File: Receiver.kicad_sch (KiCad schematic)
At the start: 18 parts, among them J3 ReceiverData, J4 ReceiverRS485, U11 MAX485E, U13 LM7805

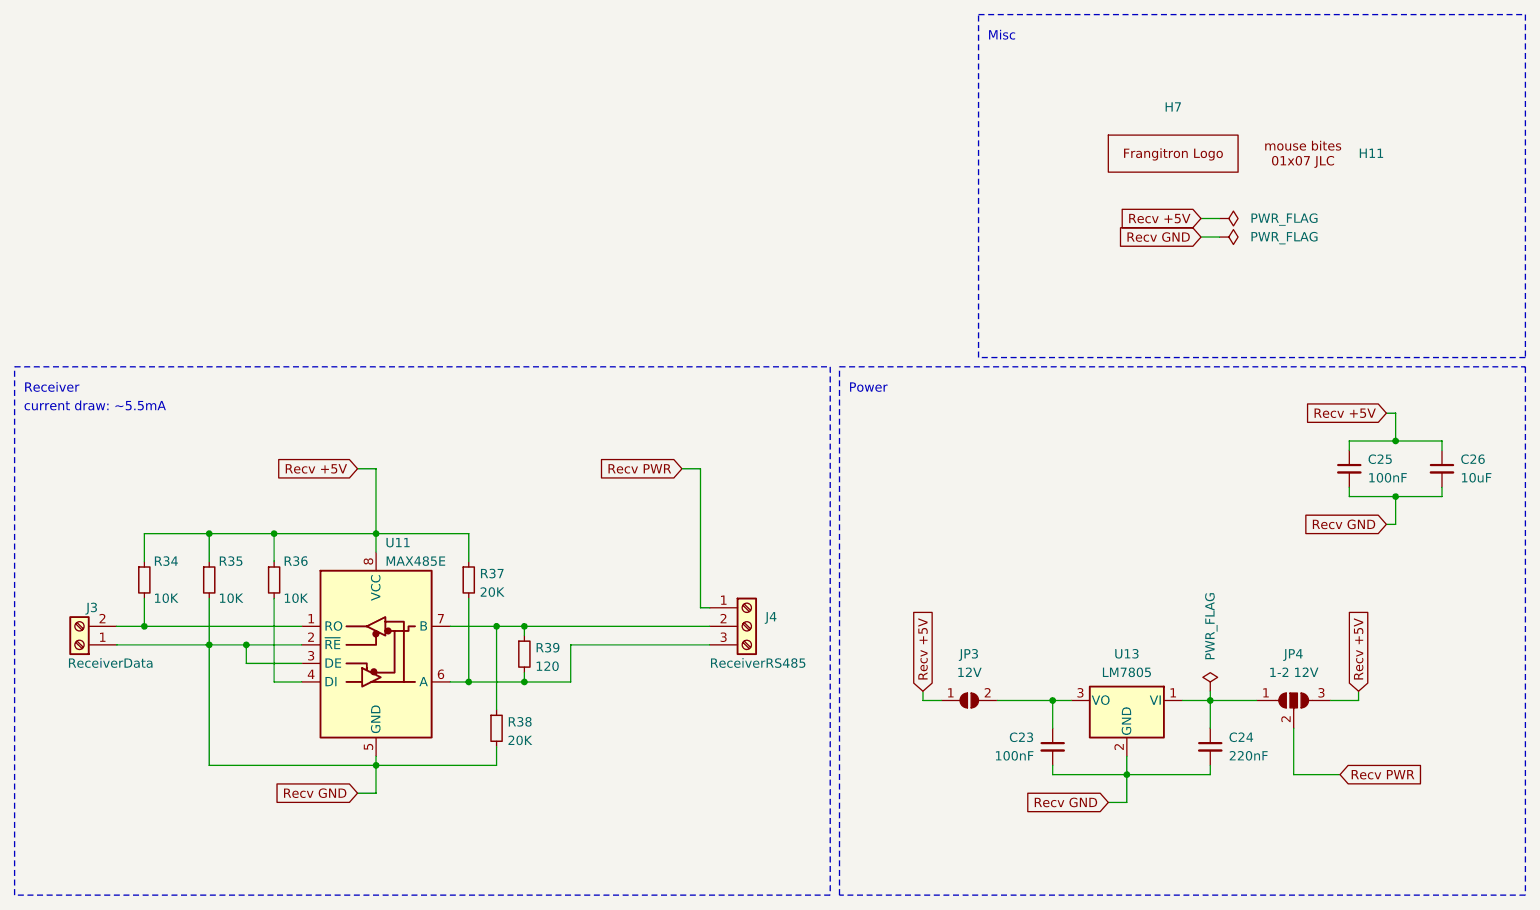
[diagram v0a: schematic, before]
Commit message: receiver layout OK, some references fixed
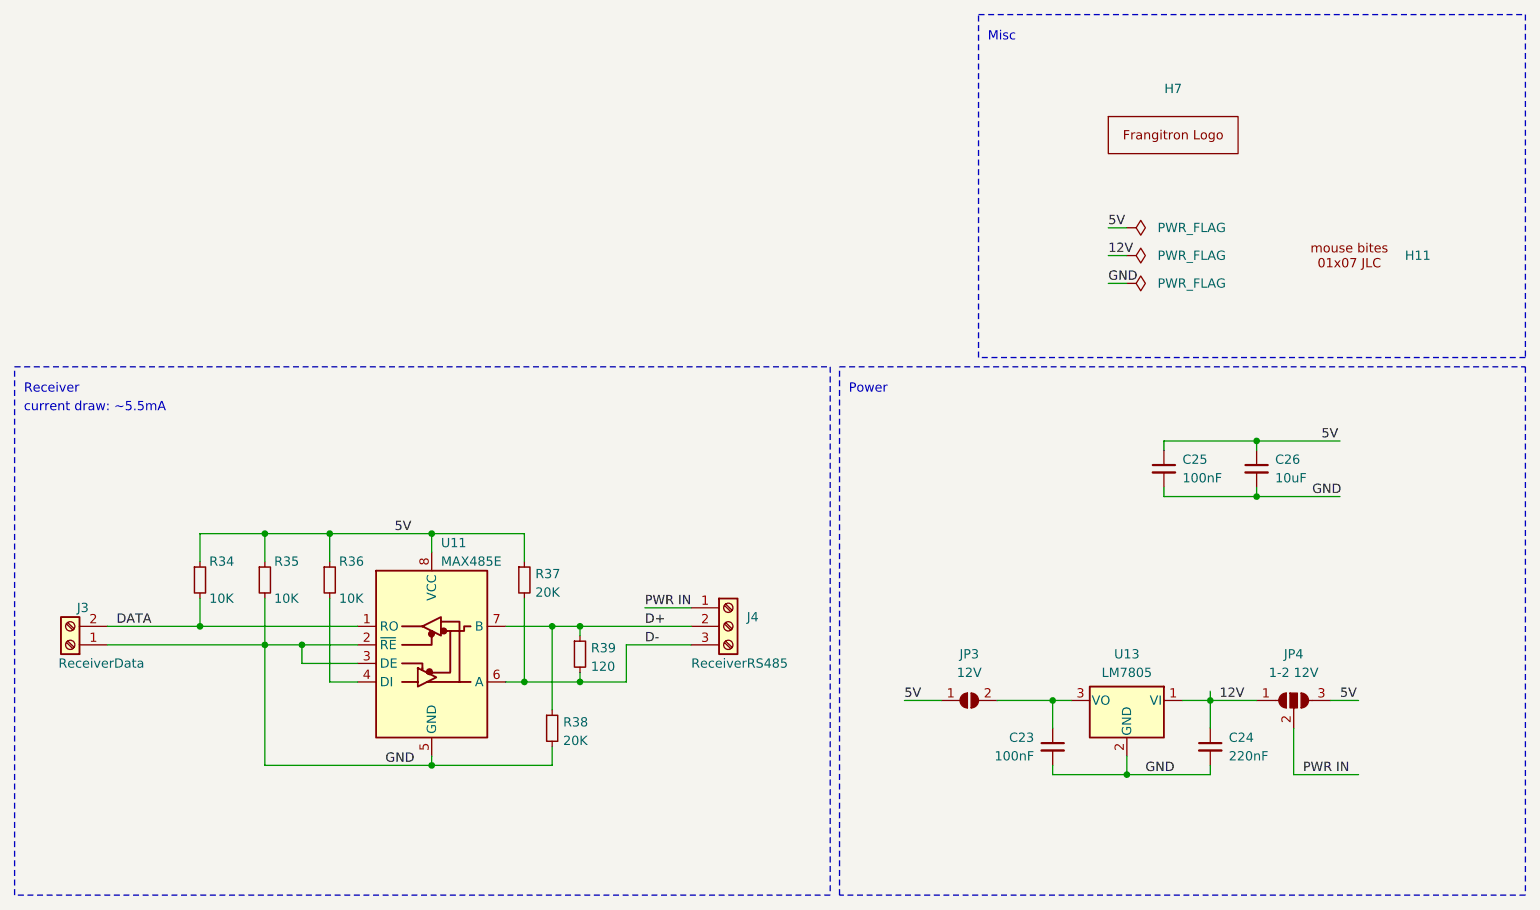
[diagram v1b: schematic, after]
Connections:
- net D+: now reaches J4.2 (Pin_2), R38.1, R39.1, U11.7 (B)
- net D-: now reaches J4.3 (Pin_3), R37.2, R39.2, U11.6 (A)
- net 12V: now reaches C24.1, JP4.1 (A), U13.1 (VI)
- net DATA: now reaches J3.2 (Pin_2), R34.2, U11.1 (RO)
- net Recv +5V renamed 5V
- net Recv GND renamed GND
- net Recv PWR renamed PWR IN
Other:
- moved on the sheet: C25, C26, H11, H7, J3, J4, R34, R35, R36, R37, R38, R39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

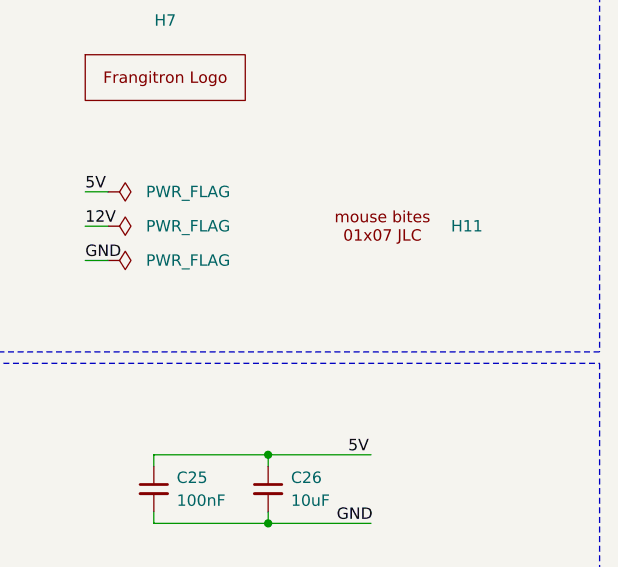
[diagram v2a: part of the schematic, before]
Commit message: panelization with only mouse bites, routing finished
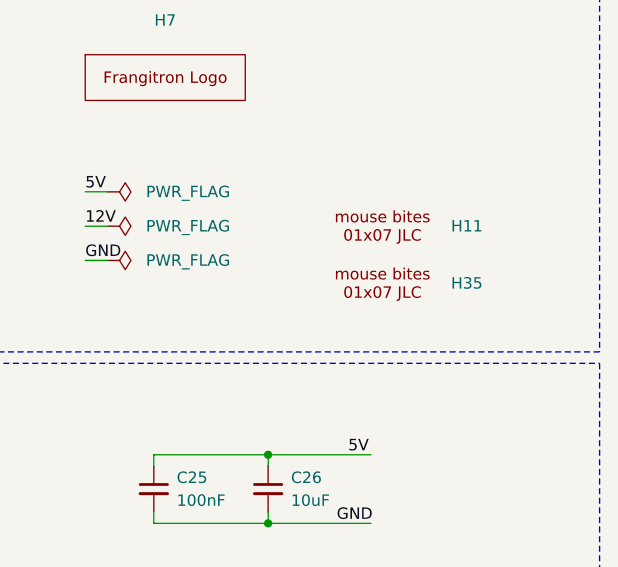
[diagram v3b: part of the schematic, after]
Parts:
- added H35: ~, Library:mouse-bites-1x07-jlc, symbol Library:mouse-bites-1x07-jlc
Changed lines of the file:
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@@
+    )
+  )
+  (symbol (lib_id "Library:mouse-bites-1x07-jlc") (at 224.79 68.58 0) (unit 1)
+    (in_bom yes) (on_board yes) (dnp no) (fields_autoplaced)
+    (property "Reference" "H35" (at 232.41 68.58 0)
+      (effects (font (size 1.27 1.27)) (justify left))
+    )
+    (property "Value" "~" (at 224.79 68.58 0)
+      (effects (font (size 1.27 1.27)))
+    )
+    (property "Footprint" "Library:mouse-bites-1x07-jlc" (at 224.79 68.58 0)
+      (effects (font (size 1.27 1.27)) hide)
+    )
+    (property "Datasheet" "" (at 224.79 68.58 0)
+      (effects (font (size 1.27 1.27)) hide)
+    )
+    (instances
+      (project "rp2040-led-board-schematics-v02"
+        (path "/c1a38541-3f06-4b3b-ba3a-decae3ac3c31/757d6d50-47c9-4cb1-8547-9b2447e826a6"
+          (reference "H35") (unit 1)
+        )
+        (path "/c1a38541-3f06-4b3b-ba3a-decae3ac3c31/c0d607bf-2e76-4853-b2ed-907dd6c894fe"
+          (reference "H36") (unit 1)
+        )
+        (path "/c1a38541-3f06-4b3b-ba3a-decae3ac3c31/45693edd-6dc6-41b8-8b1c-a9a8e5afcadf"
+          (reference "H37") (unit 1)
+        )
+        (path "/c1a38541-3f06-4b3b-ba3a-decae3ac3c31/50d6fe7a-2d25-4b6a-8e40-e76ae84b788d"
+          (reference "H38") (unit 1)
+        )
+        (path "/c1a38541-3f06-4b3b-ba3a-decae3ac3c31/62e0dde2-ad5d-4205-a74c-f24b413f3931"
+          (reference "H39") (unit 1)
+        )
+        (path "/c1a38541-3f06-4b3b-ba3a-decae3ac3c31/25bef58f-ca62-4f18-ad32-cc60a54b91e0"
+          (reference "H40") (unit 1)
+        )
+        (path "/c1a38541-3f06-4b3b-ba3a-decae3ac3c31/507a174b-d652-466e-bcdb-3655449e938c"
+          (reference "H41") (unit 1)
+        )
+        (path "/c1a38541-3f06-4b3b-ba3a-decae3ac3c31/ceb5b469-5e62-41bb-a8f0-8c2a1861cc28"
+          (reference "H42") (unit 1)
+        )
+      )
     )
   )

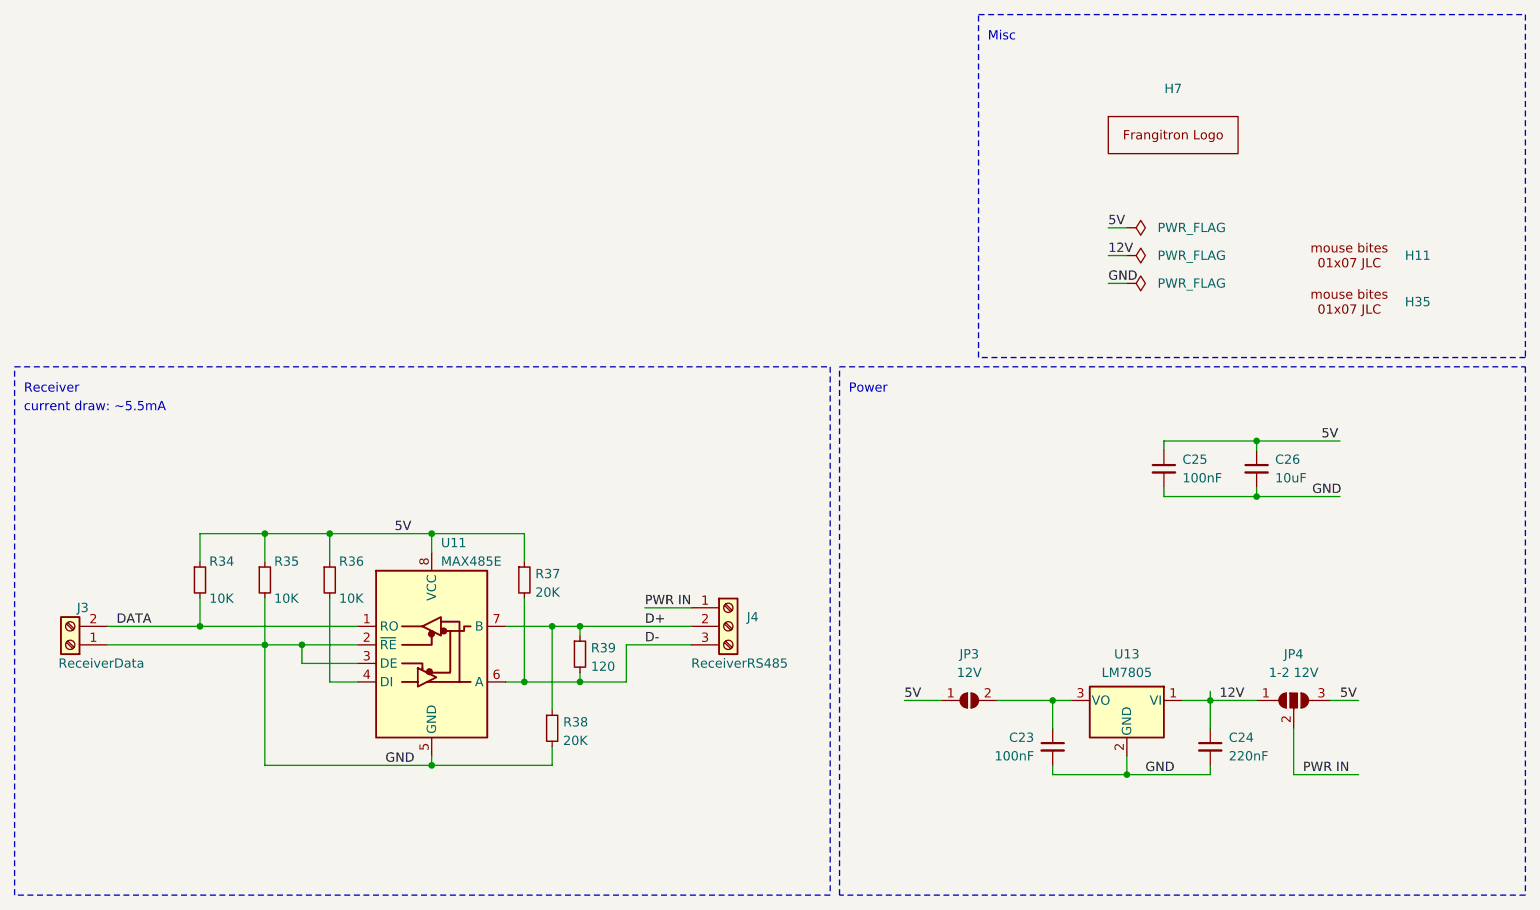
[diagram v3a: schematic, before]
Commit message: Geographically reannotate
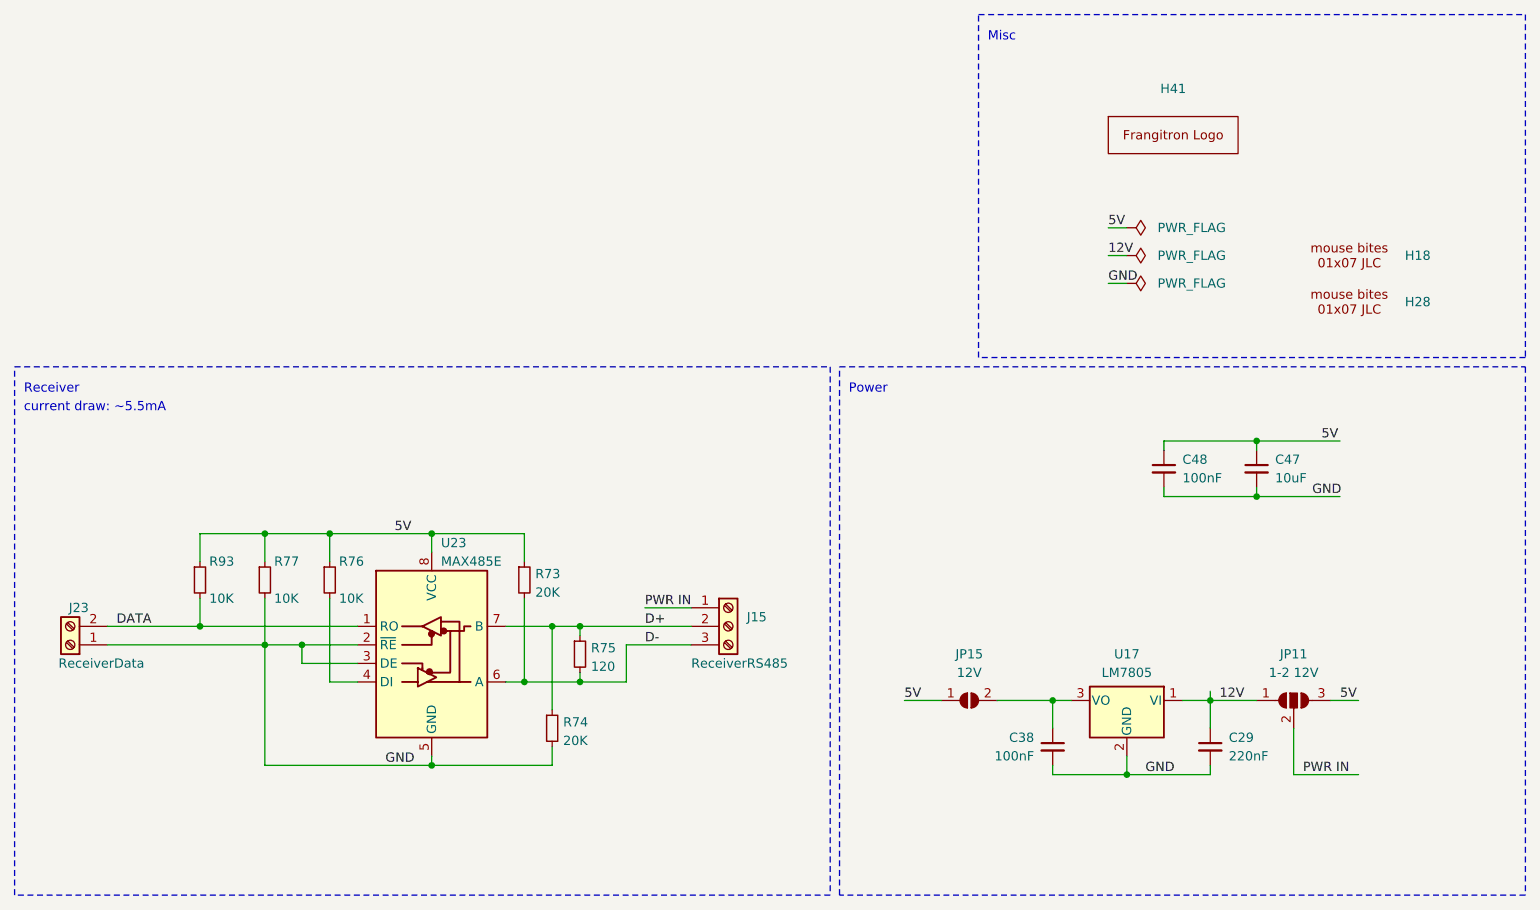
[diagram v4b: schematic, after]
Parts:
- C47: renamed from C26; footprint Capacitor_SMD:C_0402_1005Metric -> Capacitor_SMD:C_0603_1608Metric
- renumbered C24 to C29, C23 to C38, C25 to C48, H11 to H18, H35 to H28, H7 to H41, J4 to J15, J3 to J23, JP4 to JP11, JP3 to JP15, R37 to R73, R38 to R74, R39 to R75, R36 to R76, R35 to R77, R34 to R93, U13 to U17, U11 to U23

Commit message: fix power sources, update reveivers accordingly (main board PCB not updated yet)
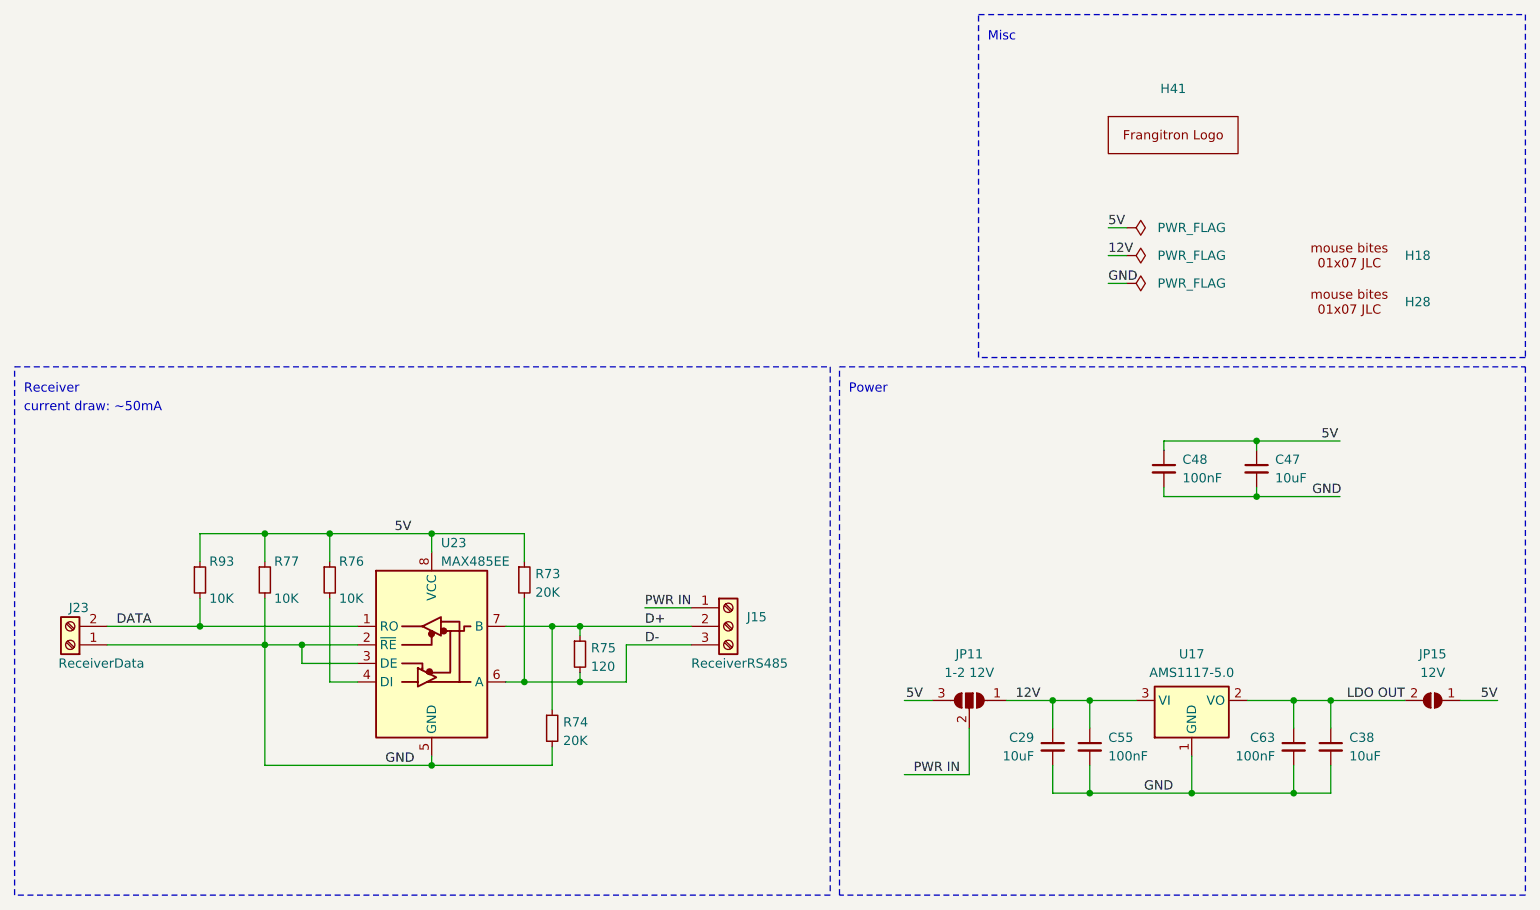
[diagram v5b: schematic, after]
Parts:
- removed U17: LM7805, Package_TO_SOT_SMD:SOT-223, symbol Regulator_Linear:LM7805_TO220
- added C55, C63: 100nF, Capacitor_SMD:C_0603_1608Metric, symbol Device:C_Small
- added U17: AMS1117-5.0, Package_TO_SOT_SMD:SOT-223-3_TabPin2, symbol Regulator_Linear:AMS1117-5.0
- C29: value 220nF -> 10uF; LCSC Part # C1525 -> (none); LCSC Part Number C1525 -> (none)
- C38: value 100nF -> 10uF; LCSC Part # C1525 -> (none); LCSC Part Number C1525 -> (none)
- C47, C48: LCSC Part # C1525 -> (none); LCSC Part Number C1525 -> (none)
- R73, R74, R75: LCSC Part # C4328 -> (none); LCSC Part Number C4328 -> (none)
- R76, R77, R93: LCSC Part # C15401 -> (none); LCSC Part Number C15401 -> (none)
- U23: value MAX485E -> MAX485EE
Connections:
- net 12V: now also C55.1, U17.3 (VI)
- net GND: now also C55.2, C63.2, U17.1 (GND)
- net LDO OUT: now reaches C38.1, JP15.2 (B)
- net LDO OUT: now also C63.1, U17.2 (VO)
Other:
- note added: "current draw: ~50mA"
- note removed: "current draw: ~5.5mA"
- moved on the sheet: C29, C38, JP11, JP15

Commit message: should be ready to find parts
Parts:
- removed C47: 10uF, Capacitor_SMD:C_0603_1608Metric, symbol Device:C_Small
- removed C48: 100nF, Capacitor_SMD:C_0603_1608Metric, symbol Device:C_Small
- added C16: 100nF, Capacitor_SMD:C_0603_1608Metric, symbol Device:C_Small
- added C19: 10uF, Capacitor_SMD:C_0603_1608Metric, symbol Device:C_Small
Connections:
- net 5V: now also C16.1, C19.1
- net GND: now also C16.2, C19.2
